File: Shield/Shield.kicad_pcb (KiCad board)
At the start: 2 copper layers, 27.9 x 20.3 mm, 3 parts, among them U1 25aa040a-i/p, U2 ESP32-S3-DevKitC

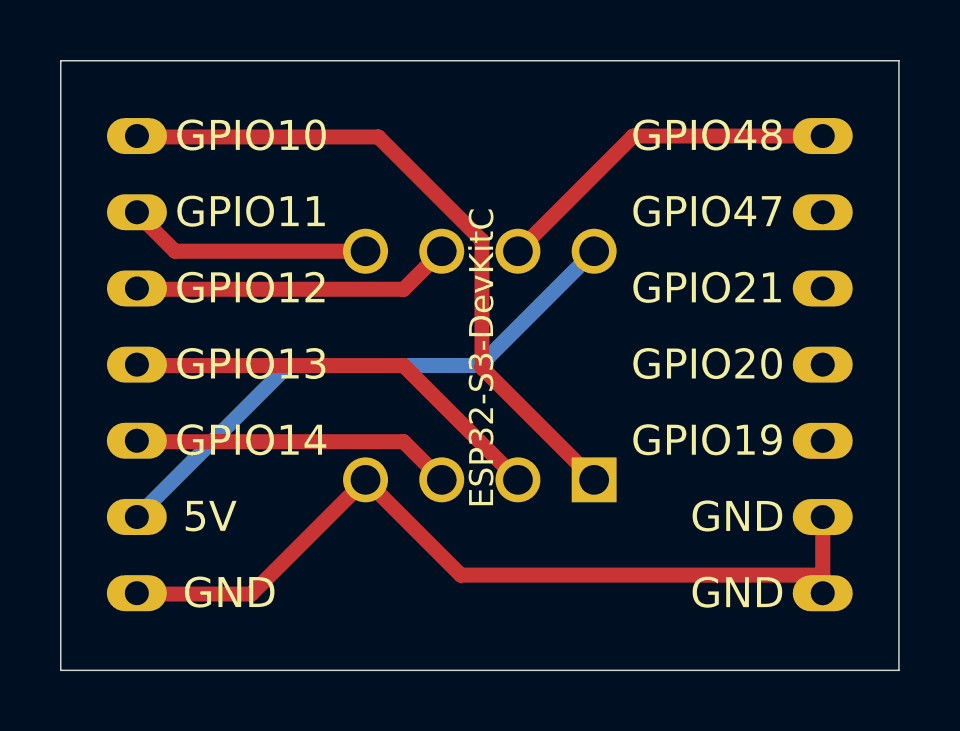
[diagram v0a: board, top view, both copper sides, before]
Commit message: change address calling
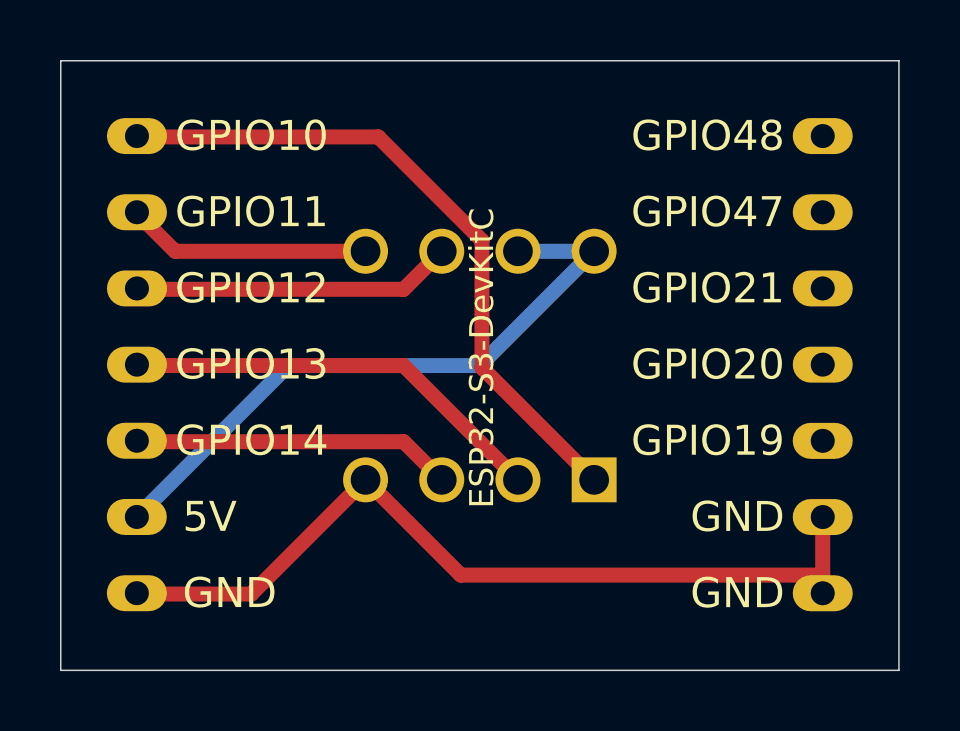
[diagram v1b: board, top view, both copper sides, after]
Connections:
- U1 pad 7: HOLD -> +5V
- U2 pad 29: HOLD -> unconnected-(U2-GPIO48-Pad29)
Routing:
- net HOLD: track 11.8 -> 0.00 mm
- net +5V: track 18.9 -> 21.5 mm
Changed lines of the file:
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@@
 	(net 10 "GND")
 	(net 11 "WP")
-	(net 12 "HOLD")
+	(net 12 "unconnected-(U2-GPIO48-Pad29)")
 	(footprint "PCM_Espressif:ESP32-S3-DevKitC"
 		(layer "F.Cu")
@@
 			(net 3 "unconnected-(U2-GPIO19{slash}USB_D--Pad25)")
 			(pinfunction "GPIO19/USB_D-")
-			(pintype "bidirectional")
+			(pintype "bidirectional+no_connect")
 		)
 		(pad "26" thru_hole oval
@@
 			(net 5 "unconnected-(U2-GPIO20{slash}USB_D+-Pad26)")
 			(pinfunction "GPIO20/USB_D+")
-			(pintype "bidirectional")
+			(pintype "bidirectional+no_connect")
 		)
 		(pad "27" thru_hole oval
@@
 			(net 4 "unconnected-(U2-GPIO21-Pad27)")
 			(pinfunction "GPIO21")
-			(pintype "bidirectional")
+			(pintype "bidirectional+no_connect")
 		)
 		(pad "28" thru_hole oval
@@
 			(net 1 "unconnected-(U2-GPIO47-Pad28)")
 			(pinfunction "GPIO47")
-			(pintype "bidirectional")
+			(pintype "bidirectional+no_connect")
 		)
 		(pad "29" thru_hole oval
@@
 			(layers "*.Cu" "*.Mask")
 			(remove_unused_layers no)
-			(net 12 "HOLD")
+			(net 12 "unconnected-(U2-GPIO48-Pad29)")
 			(pinfunction "GPIO48")
-			(pintype "bidirectional")
+			(pintype "bidirectional+no_connect")
 		)
 	)
@@
 			(layer "B.Fab")
 		)
-		(fp_text user "*"
-			(at 0.508 0 -90)
-			(layer "B.Fab")
-			(effects
-				(font
-					(size 1 1)
-					(thickness 0.15)
-				)
-				(justify mirror)
-			)
-		)
 		(fp_text user "${REFERENCE}"
 			(at 3.81 -3.81 -90)
 			(unlocked yes)
+			(layer "B.Fab")
+			(effects
+				(font
+					(size 1 1)
+					(thickness 0.15)
+				)
+				(justify mirror)
+			)
+		)
+		(fp_text user "*"
+			(at 0.508 0 -90)
 			(layer "B.Fab")
 			(effects
@@
 			(layers "*.Cu" "*.Mask")
 			(remove_unused_layers no)
-			(net 12 "HOLD")
+			(net 9 "+5V")
 			(pinfunction "HOLD*")
 			(pintype "input")
@@
 	)
 	(segment
+		(start 120.65 92.075)
+		(end 123.19 92.075)
+		(width 0.5)
+		(layer "B.Cu")
+		(net 9)
+	)
+	(segment
 		(start 119.38 95.885)
 		(end 112.9936 95.885)
@@
 		(net 11)
 	)
-	(segment
-		(start 124.49 88.235)
-		(end 130.81 88.235)
-		(width 0.5)
-		(layer "F.Cu")
-		(net 12)
-	)
-	(segment
-		(start 120.65 92.075)
-		(end 124.49 88.235)
-		(width 0.5)
-		(layer "F.Cu")
-		(net 12)
-	)
 )

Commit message: Added level shifter
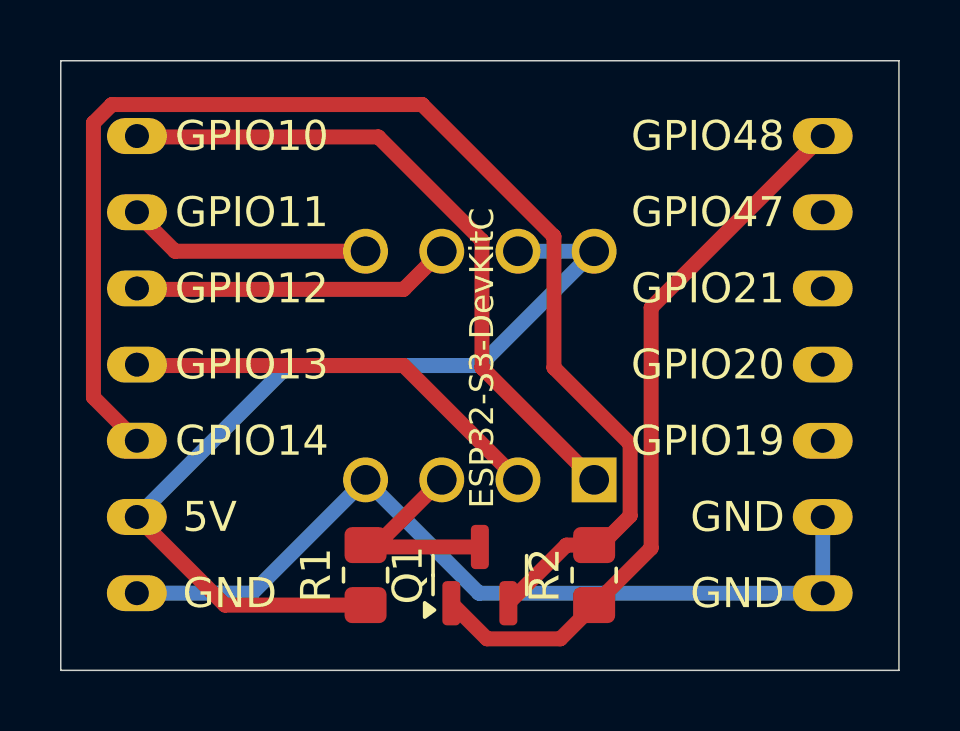
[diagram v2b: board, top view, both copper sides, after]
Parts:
- added Q1: BSS138, Package_TO_SOT_SMD:SOT-23, F.Cu at (119.4, 102.9)
- added R1: R_US, Resistor_SMD:R_0805_2012Metric_Pad1.20x1.40mm_HandSolder, F.Cu at (115.6, 102.9)
- added R2: R_US, Resistor_SMD:R_0805_2012Metric_Pad1.20x1.40mm_HandSolder, F.Cu at (123.2, 102.9)
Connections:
- U1 pad 3: WP -> HVWP
- U2 pad 20: WP -> LVWP
- U2 pad 29: unconnected-(U2-GPIO48-Pad29) -> +3V3
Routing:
- net LVWP: track 0.00 -> 44.2 mm
- net +3V3: track 0.00 -> 24.5 mm
- net WP: track 10.7 -> 0.00 mm
- net +5V: track 21.5 -> 30.3 mm
- net HVWP: track 0.00 -> 6.58 mm
